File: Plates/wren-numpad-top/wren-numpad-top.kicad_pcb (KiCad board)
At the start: 2 copper layers, 220 x 112.8 mm, 52 parts

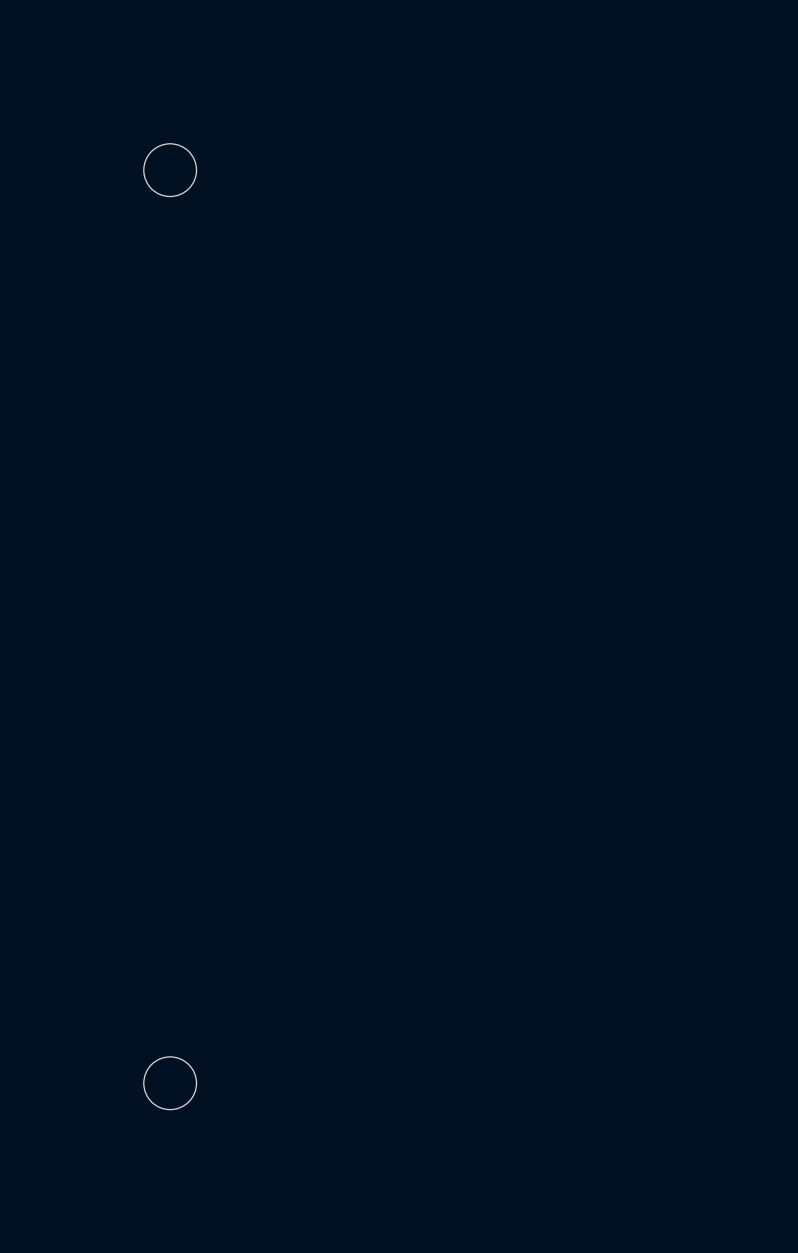
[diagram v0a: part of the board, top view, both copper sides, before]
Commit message: Update screw positions on plates to match universal PCBs, update Gerbers
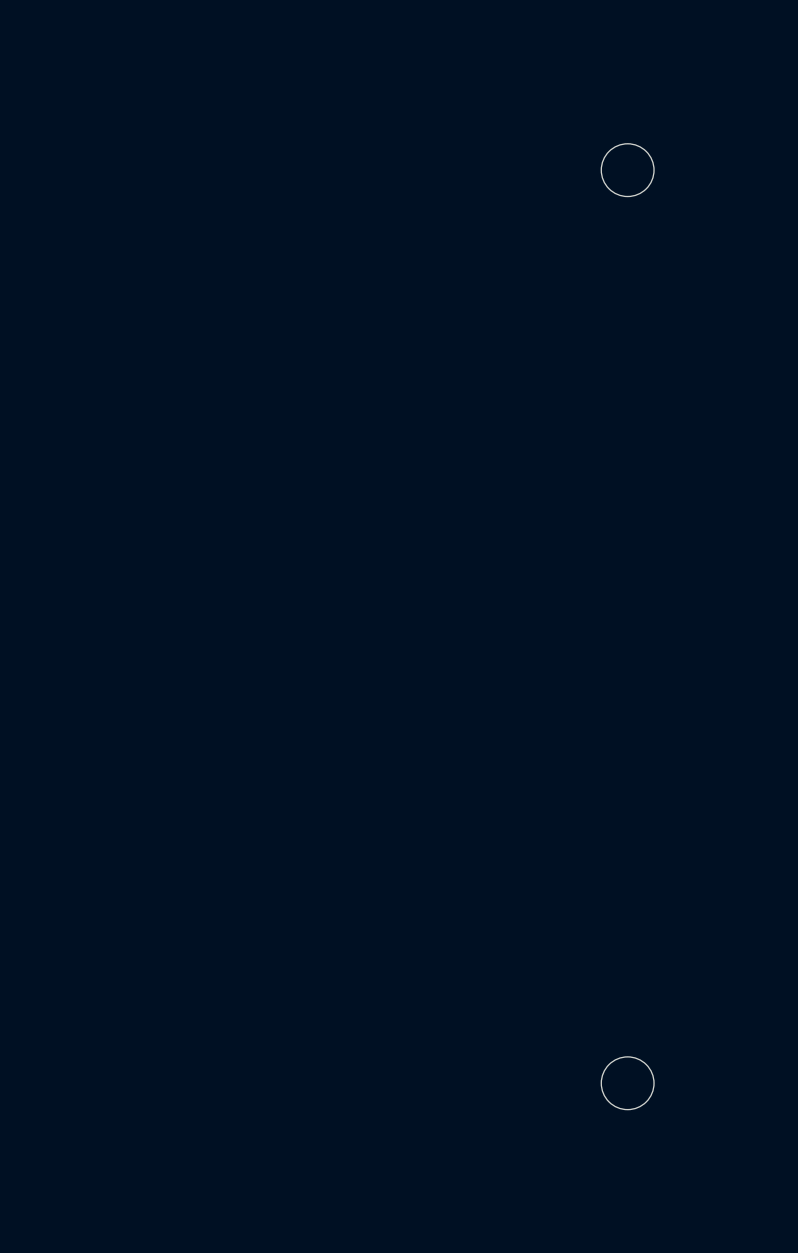
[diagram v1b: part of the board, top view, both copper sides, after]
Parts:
- moved H1 19.1 mm to (75.4, 46.0)
- moved H4 19.1 mm to (75.4, 84.1)

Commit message: Create .svg for top plates
On realizing that my PCB plates weren't really manufacturable, I decided to use those KiCad files to make a .svg of my plate design that could be laser cut by services like SendCutSend.
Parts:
- removed REF**: MX_Stabilizer_Cutout-2u, footprints:MX_Stabilizer_Cutout-2u
- MX1, MX10, MX11, MX12, MX13, MX14, MX15, MX16, MX17, MX18, MX19, MX2, MX20, MX21, MX22, MX23, MX24, MX25, MX26, MX27, MX28, MX29, MX3, MX30, MX31, MX32, MX33, MX34, MX35, MX36, MX37, MX38, MX39, MX4, MX40, MX42, MX43, MX44, MX5, MX6, MX7, MX8, MX9: footprint footprints:MX_Switch_Cutout -> footprints:MX-Alps_Switch_Cutout
- MX41: footprint footprints:MX_Switch_Cutout -> footprints:MX-Alps_Switch_Cutout-1u_2u
- turned MX41 to 240 degrees
